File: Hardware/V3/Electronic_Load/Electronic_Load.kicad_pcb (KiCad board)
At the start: 4 copper layers, 160 x 100 mm, 103 parts, among them J101 DIN41612_02x32_AC, J301 Address, J302 SWD, J401 FAN_1, J402 FAN_2, J501 IN_1, J502 IN_2, Q301 BSS138, Q302 BSS138, Q401 DMG 1012UW7 DII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

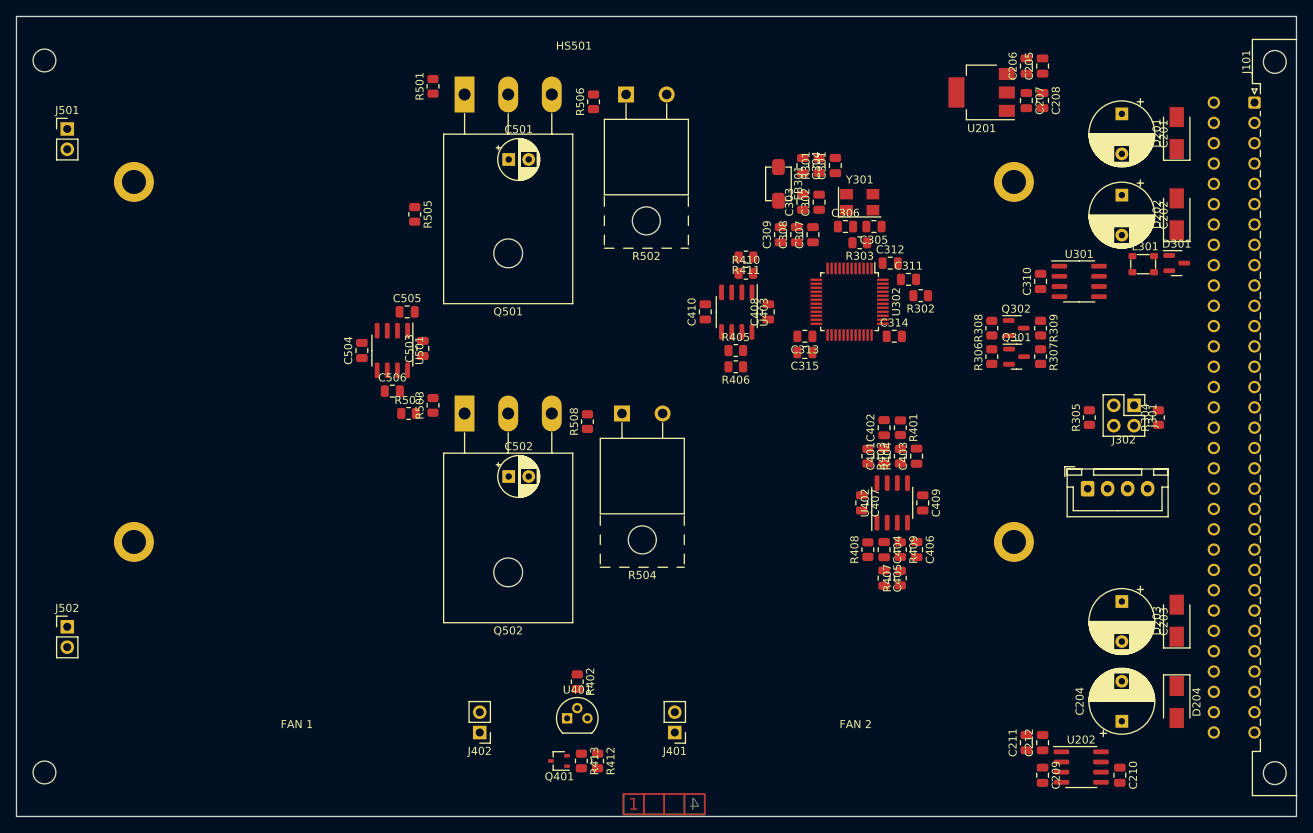
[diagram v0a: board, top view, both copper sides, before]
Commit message: finalize electronic load; Readme Update
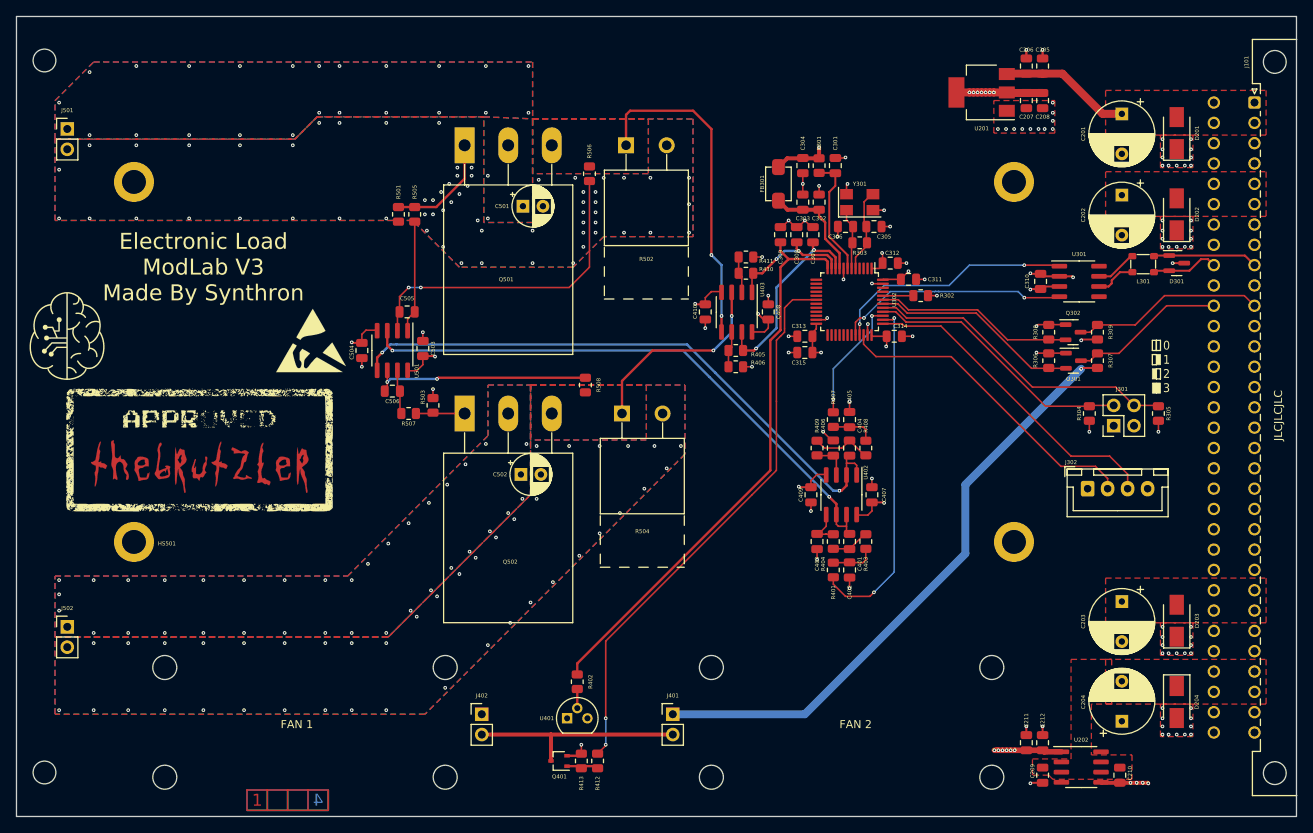
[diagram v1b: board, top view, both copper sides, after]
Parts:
- added ?: , , F.Cu at (146.1, 121.4)
- added ?: , , F.Cu at (112.8, 135.1)
- added ?: , , F.Cu at (146.1, 135.1)
- added ?: , , F.Cu at (181.1, 135.1)
- added ?: , , F.Cu at (112.8, 121.4)
- added ?: , , F.Cu at (77.7, 121.4)
- added ?: , , F.Cu at (181.1, 121.4)
- added ?: , , F.Cu at (77.7, 135.1)
- added G***: LOGO, TheBrutzlers_Lib:thebrutzler_approved_small02, F.Cu at (82.0, 94.2)
- added G***: LOGO, eigene:logo, F.Cu at (65.5, 80.0)
- added REF**: ESD-Logo_8.9x8mm_SilkScreen, Symbol:ESD-Logo_8.9x8mm_SilkScreen, F.Cu at (96.0, 80.5)
- moved ? 47.1 mm to (87.6, 142.7)
- moved R407 21.5 mm to (161.3, 90.4), turned to -90 degrees
- moved C405 20.3 mm to (163.3, 90.4), turned to 90 degrees
- moved R401 19.7 mm to (161.3, 109.2), turned to 90 degrees
- moved C402 18.3 mm to (163.3, 109.2), turned to -90 degrees
- moved R501 16.6 mm to (106.9, 64.8), turned to -90 degrees
- moved C406 16.4 mm to (161.3, 94.0), turned to 90 degrees
- moved R409 16.4 mm to (159.3, 94.0)
- moved C403 16.4 mm to (159.3, 105.7), turned to -90 degrees
- moved C409 14.0 mm to (158.5, 99.8), turned to 90 degrees
- moved R404 13.6 mm to (161.3, 105.7)
- moved C404 13.4 mm to (163.3, 94.0)
- moved R408 12.7 mm to (165.4, 94.0), turned to -90 degrees
- moved C401 11.5 mm to (163.3, 105.7)
- moved R403 10.7 mm to (165.4, 105.7), turned to 90 degrees
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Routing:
- net +5V: track 0.00 -> 157.9 mm, vias 0 -> 2
- net /Load/I_SET_CH2: track 0.00 -> 75.3 mm, vias 0 -> 2
- net /Load/I_SET_CH1: track 0.00 -> 72.7 mm, vias 0 -> 2
- net /CPU/TEMP: track 0.00 -> 71.2 mm
- net /CPU/FAN_EN: track 0.00 -> 69.8 mm, vias 0 -> 2
- net GND: track 0.00 -> 68.2 mm, vias 0 -> 206
- net +3V3: track 0.00 -> 43.9 mm, vias 0 -> 15
- net /CPU/PWM_CH1: track 0.00 -> 43.6 mm, vias 0 -> 2
- net /Load/I_IN_CH1: track 0.00 -> 41.5 mm, vias 0 -> 2
- net Net-(U501-Pad2): track 0.00 -> 40.4 mm, vias 0 -> 2
- net /CPU/SWCLK: track 0.00 -> 40.2 mm
- net /CPU/SWDIO: track 0.00 -> 39.9 mm
- net Net-(J301-Pad4): track 0.00 -> 39.5 mm
- net Net-(J301-Pad2): track 0.00 -> 33.8 mm
- net CAN_Tx: track 0.00 -> 30.5 mm, vias 0 -> 2
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- added copper zone on F.Cu, net +15V
- added copper zone on In1.Cu, net +15V
- added copper zone on F.Cu, net +24V
- added copper zone on In1.Cu, net +3V3
- added copper zone on F.Cu, net +5V
- added copper zone on F.Cu, net -15V
- added copper zone on In1.Cu, net -5V
- added copper zone on B.Cu, net /Load/I_IN_CH1
- added copper zone on F.Cu, net /Load/I_IN_CH1
- added copper zone on In1.Cu, net /Load/I_IN_CH1
- added copper zone on In2.Cu, net /Load/I_IN_CH1
- added copper zone on B.Cu, net /Load/I_IN_CH2
- added copper zone on F.Cu, net /Load/I_IN_CH2
- added copper zone on In1.Cu, net /Load/I_IN_CH2
- added copper zone on In2.Cu, net /Load/I_IN_CH2
- added copper zone on B.Cu, net GND
- added copper zone on F.Cu, net GND
- added copper zone on In1.Cu, net GND
- added copper zone on In2.Cu, net GND
- added copper zone on B.Cu, net Net-(C501-Pad1)
- added copper zone on F.Cu, net Net-(C501-Pad1)
- added copper zone on In1.Cu, net Net-(C501-Pad1)
- added copper zone on In2.Cu, net Net-(C501-Pad1)
- added copper zone on B.Cu, net Net-(C502-Pad1)
- added copper zone on F.Cu, net Net-(C502-Pad1)
- added copper zone on In1.Cu, net Net-(C502-Pad1)
- added copper zone on In2.Cu, net Net-(C502-Pad1)
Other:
- board text added: "0 1 2 3"
- board text added: "Electronic Load ModLab V3 Made By Synthron"
- board text added: "JLCJLCJLC"
